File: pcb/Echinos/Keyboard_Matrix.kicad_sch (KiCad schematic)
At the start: 50 parts, among them SW111 SW_Push, SW112 SW_Push, SW113 SW_Push, SW114 SW_Push, SW115 SW_Push, SW122 SW_Push, SW123 SW_Push, SW124 SW_Push, SW125 SW_Push, SW131 SW_Push, SW132 SW_Push, SW133 SW_Push, SW134 SW_Push, SW141 SW_Push, SW142 SW_Push, SW143 SW_Push, SW144 SW_Push, SW145 SW_Push, SW151 SW_Push, SW152 SW_Push, SW153 SW_Push, SW154 SW_Push, SW155 SW_Push

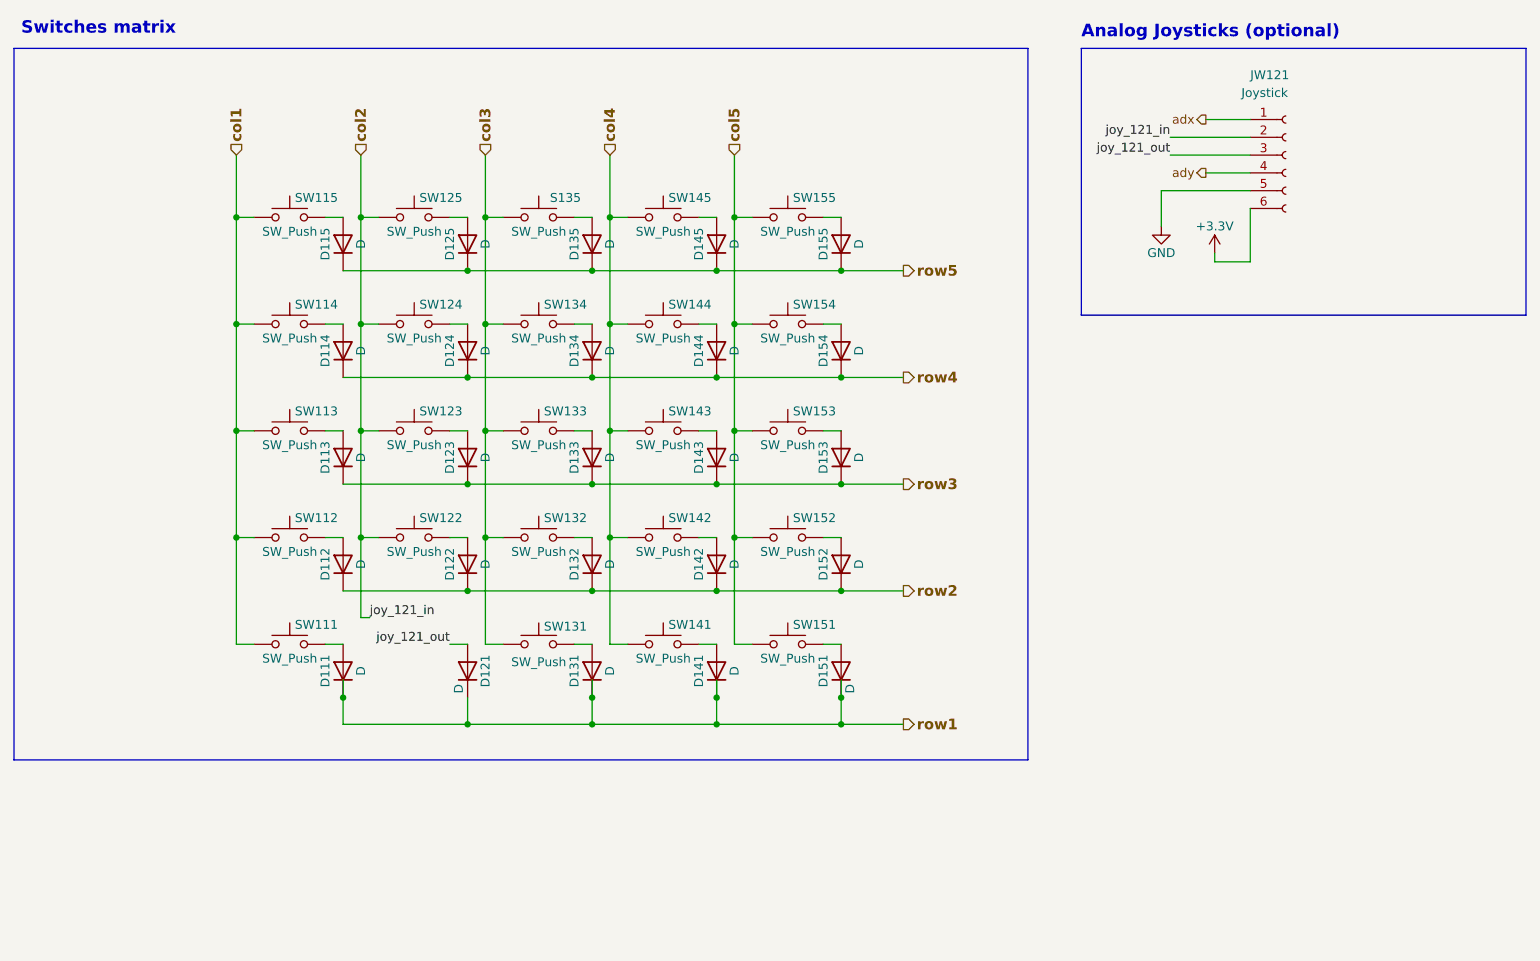
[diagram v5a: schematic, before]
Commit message: [PCB] - Save last state with Helios MCU board and gasket tabs on PCB.
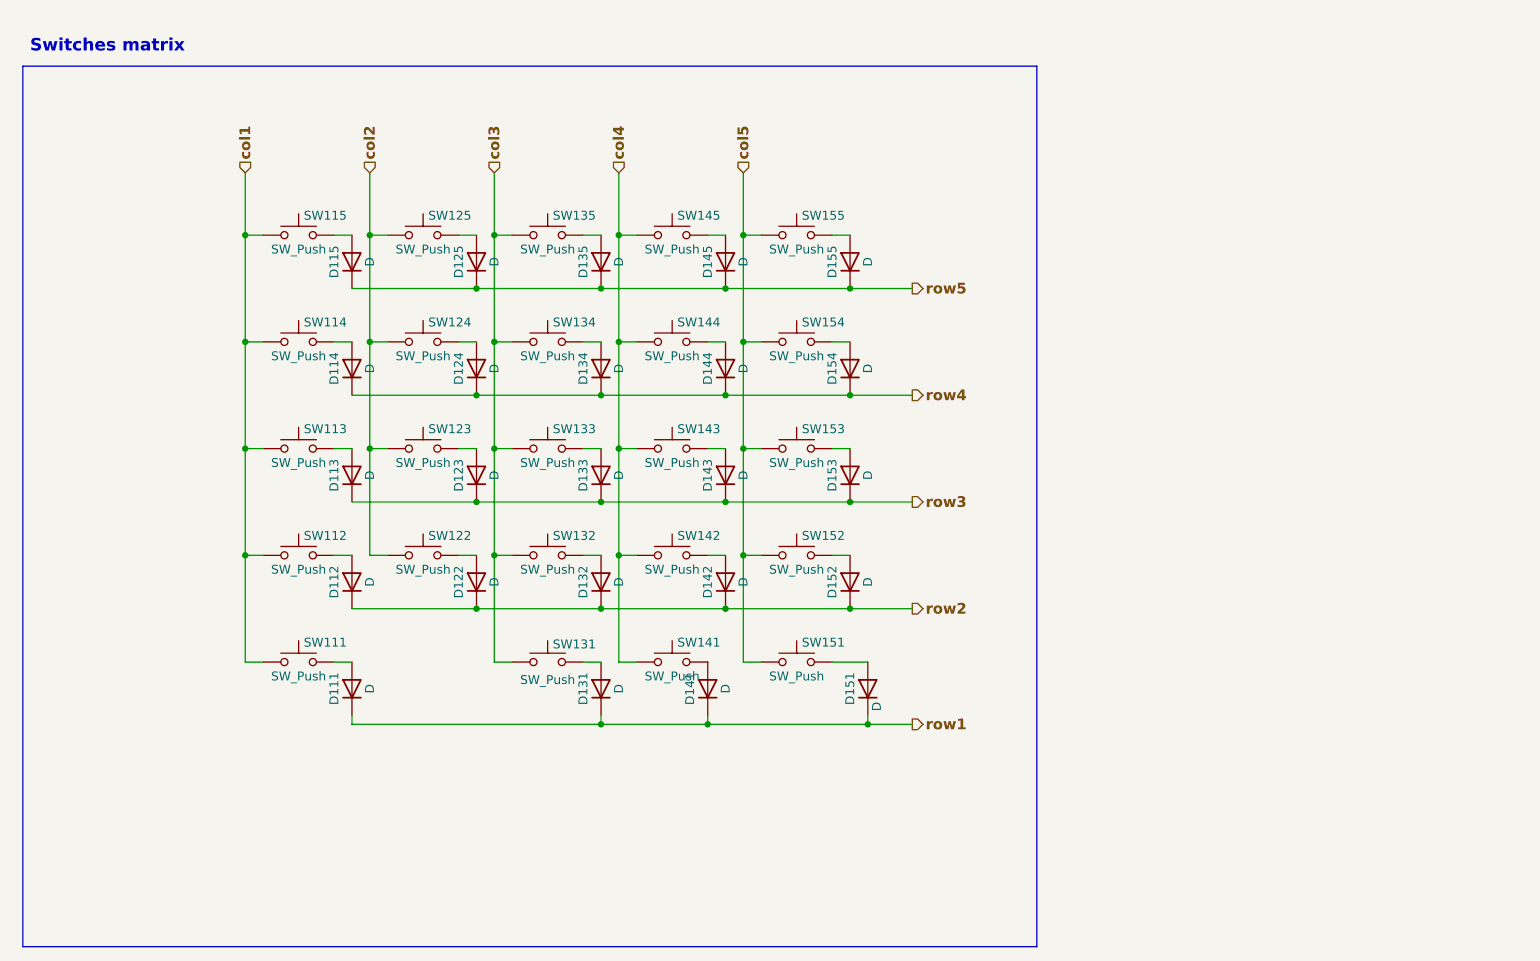
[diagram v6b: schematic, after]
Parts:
- removed D121: D, Echinos:D_SOD123, symbol Device:D
- removed JW121: Joystick, Echinos:Joystick_KSilver_JP19, symbol Connector:Conn_01x06_Socket
- D111, D112, D113, D114, D115, D122, D123, D124, D125, D131, D132, D133, D134, D135, D141, D142, D143, D144, D145, D151, D152, D153, D154, D155: LCSC C369920 -> C109203; LCSC2 (none) -> C909967
- SW111, SW113, SW114, SW115, SW122: footprint Echinos:SW_Choc_MX_KS33_1u_hotswap -> Echinos:SW_Choc_MX_KS33_1u_TH_hotswap; FT Layer Override (none) -> bottom; FT Position Offset (none) -> 0.0,0.0; LCSC (none) -> C5333465; now left out of the parts list
- SW112, SW123, SW124, SW125, SW131, SW132, SW133, SW134, SW141, SW142, SW143, SW144, SW145, SW151, SW152, SW153, SW154, SW155: footprint Echinos:SW_Choc_MX_KS33_1u_hotswap -> Echinos:SW_Choc_MX_KS33_1u_TH_hotswap; FT Layer Override (none) -> bottom; FT Position Offset (none) -> 0.0,0.0; LCSC (none) -> C5333465
- SW135: renamed from S135; footprint Echinos:SW_Choc_MX_KS33_1u_hotswap -> Echinos:SW_Choc_MX_KS33_1u_TH_hotswap; FT Layer Override (none) -> bottom; FT Position Offset (none) -> 0.0,0.0; LCSC (none) -> C5333465
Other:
- note removed: "Analog Joysticks (optional)"
- moved on the sheet: D111, D112, D113, D114, D115, D122, D123, D124, D125, D131, D132, D133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
